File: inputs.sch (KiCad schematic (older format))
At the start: 67 parts, among them J21 Conn_01x02, J22 Conn_01x02, J23 Conn_01x02, J24 Conn_01x03, J25 Conn_01x03, J26 Conn_01x03, J27 Conn_01x03, J28 Conn_01x03, J29 Conn_01x03, J31 Conn_01x04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

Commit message: Move board thermistor, move LED resistors, add diode to probe input, NC header on probe input, change pullup on probe input, change value of enable resistor for fet driver, add ideal diode to schmatic, add fiducials to board, swap T1 and T4 opamp output
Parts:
- added D31: D, Diodes_SMD:D_SOD-323, symbol Device:D
- JP7: footprint Jumper:SolderJumper-2_P1.3mm_Open_RoundedPad1.0x1.5mm -> kicad-footprints-master:SolderJumper-2_P1.3mm_Bridged_RoundedPad1.0x1.5mm; symbol Jumper:SolderJumper_2_Open -> Jumper:SolderJumper_2_Bridged
- R34: value 10k -> 1k
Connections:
- net 3V3_LIMIT_IN: no longer JP7.1 (A)
- net 5V_LIMIT_IN: now also JP7.1 (A)
- net at U12.1, U12.2 (-): now also RN9.5 (R4.2); no longer RN9.8 (R1.2)
- net at U12.13 (-), U12.14: now also RN9.8 (R1.2); no longer RN9.5 (R4.2)
- net at R34.1: now also D31.1 (K); no longer JP7.2 (B)
- new net: D31.2 (A), JP7.2 (B)

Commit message: Adapt 2590 board layout to ideal diodes and dual power input connector
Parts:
- D31: footprint Diodes_SMD:D_SOD-323 -> Diode_SMD:D_SOD-323
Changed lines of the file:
@@
 $Descr A4 11693 8268
 encoding utf-8
-Sheet 8 13
+Sheet 4 13
 Title ""
 Date ""
@@
 F 0 "D31" H 2125 7333 50  0000 C CNN
 F 1 "D" H 2125 7424 50  0000 C CNN
-F 2 "Diodes_SMD:D_SOD-323" H 2125 7550 50  0001 C CNN
+F 2 "Diode_SMD:D_SOD-323" H 2125 7550 50  0001 C CNN
 F 3 "~" H 2125 7550 50  0001 C CNN
 	1    2125 7550

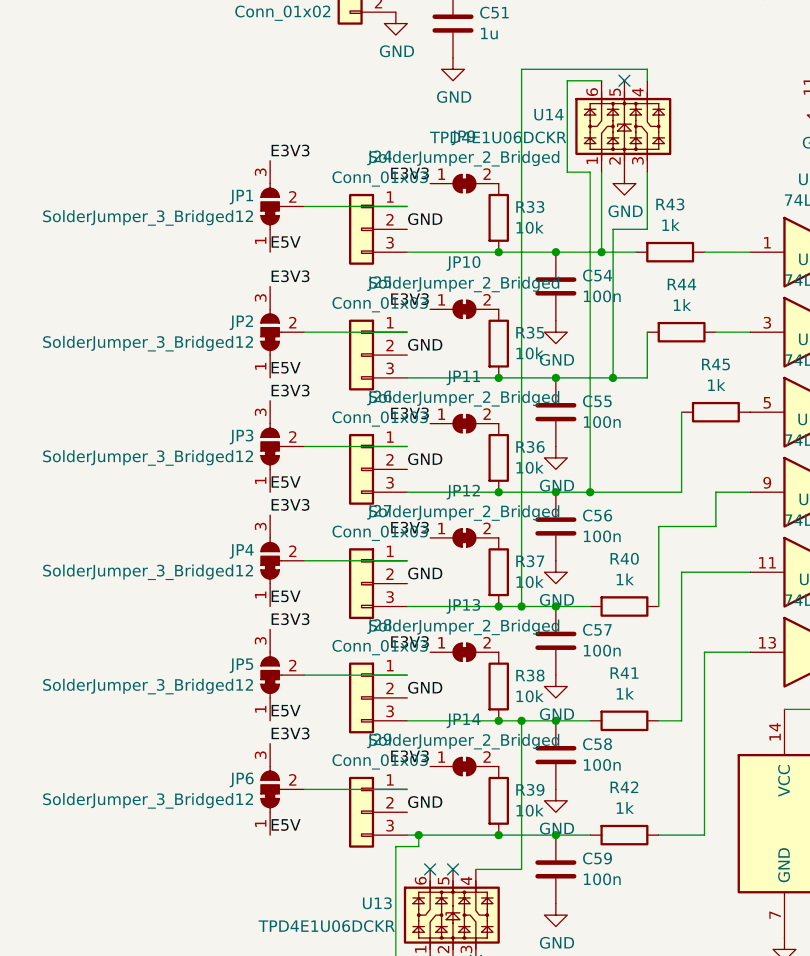
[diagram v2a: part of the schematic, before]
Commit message: Fix JP7 footprint, fix silk, add traces to vfet header
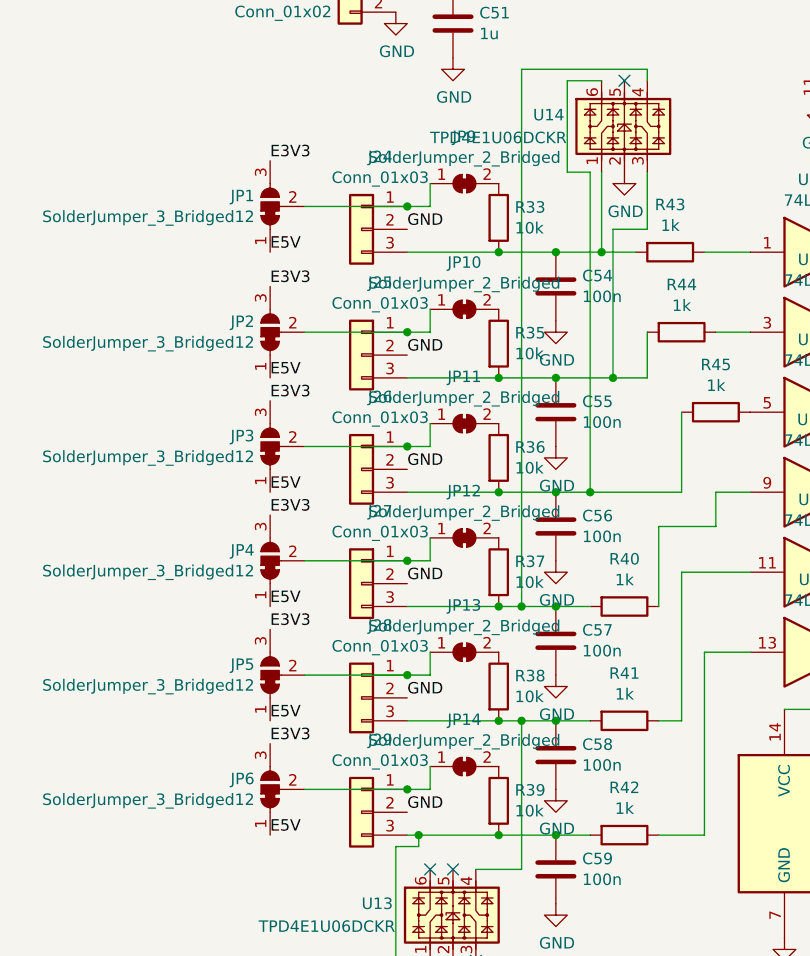
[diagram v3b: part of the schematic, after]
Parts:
- JP7: footprint kicad-footprints-master:SolderJumper-2_P1.3mm_Bridged_RoundedPad1.0x1.5mm -> Jumper:SolderJumper-2_P1.3mm_Bridged_RoundedPad1.0x1.5mm
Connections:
- net 3V3_LIMIT_IN: no longer JP10.1 (A), JP11.1 (A), JP12.1 (A), JP13.1 (A), JP14.1 (A), JP9.1 (A)
- net at J24.1 (Pin_1), JP1.2 (C): now also JP9.1 (A)
- net at J25.1 (Pin_1), JP2.2 (C): now also JP10.1 (A)
- net at J26.1 (Pin_1), JP3.2 (C): now also JP11.1 (A)
- net at J27.1 (Pin_1), JP4.2 (C): now also JP12.1 (A)
- net at J28.1 (Pin_1), JP5.2 (C): now also JP13.1 (A)
- net at J29.1 (Pin_1), JP6.2 (C): now also JP14.1 (A)
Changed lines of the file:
@@
 Wire Wire Line
 	1900 7050 2350 7050
-Text Label 2450 3300 2    50   ~ 0
-E3V3
-Text Label 2450 3850 2    50   ~ 0
-E3V3
-Text Label 2450 4350 2    50   ~ 0
-E3V3
-Text Label 2450 4850 2    50   ~ 0
-E3V3
-Text Label 2450 5350 2    50   ~ 0
-E3V3
-Text Label 2450 5850 2    50   ~ 0
-E3V3
 Wire Wire Line
 	2350 7250 2550 7250
@@
 F 0 "JP7" H 1825 7755 50  0000 C CNN
 F 1 "SolderJumper_2_Bridged" H 1825 7664 50  0000 C CNN
-F 2 "kicad-footprints-master:SolderJumper-2_P1.3mm_Bridged_RoundedPad1.0x1.5mm" H 1825 7550 50  0001 C CNN
+F 2 "Jumper:SolderJumper-2_P1.3mm_Bridged_RoundedPad1.0x1.5mm" H 1825 7550 50  0001 C CNN
 F 3 "~" H 1825 7550 50  0001 C CNN
 	1    1825 7550
@@
 Wire Wire Line
 	2275 7550 2550 7550
+Wire Wire Line
+	2350 3950 2450 3950
+Wire Wire Line
+	2450 3950 2450 3850
+Connection ~ 2350 3950
+Wire Wire Line
+	2450 3300 2450 3400
+Wire Wire Line
+	2450 3400 2350 3400
+Connection ~ 2350 3400
+Wire Wire Line
+	2350 4450 2450 4450
+Wire Wire Line
+	2450 4450 2450 4350
+Connection ~ 2350 4450
+Wire Wire Line
+	2350 4950 2450 4950
+Wire Wire Line
+	2450 4950 2450 4850
+Connection ~ 2350 4950
+Wire Wire Line
+	2350 5450 2450 5450
+Wire Wire Line
+	2450 5450 2450 5350
+Connection ~ 2350 5450
+Wire Wire Line
+	2350 5950 2450 5950
+Wire Wire Line
+	2450 5950 2450 5850
+Connection ~ 2350 5950
 $EndSCHEMATC
